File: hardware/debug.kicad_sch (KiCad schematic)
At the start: 39 parts, among them J38 Conn_01x08_Pin, J39 Conn_01x03_Pin, J40 Conn_01x08_Pin, J41 Conn_01x08_Pin, U20 74HC244, U21 74HC244, U22 74HC244

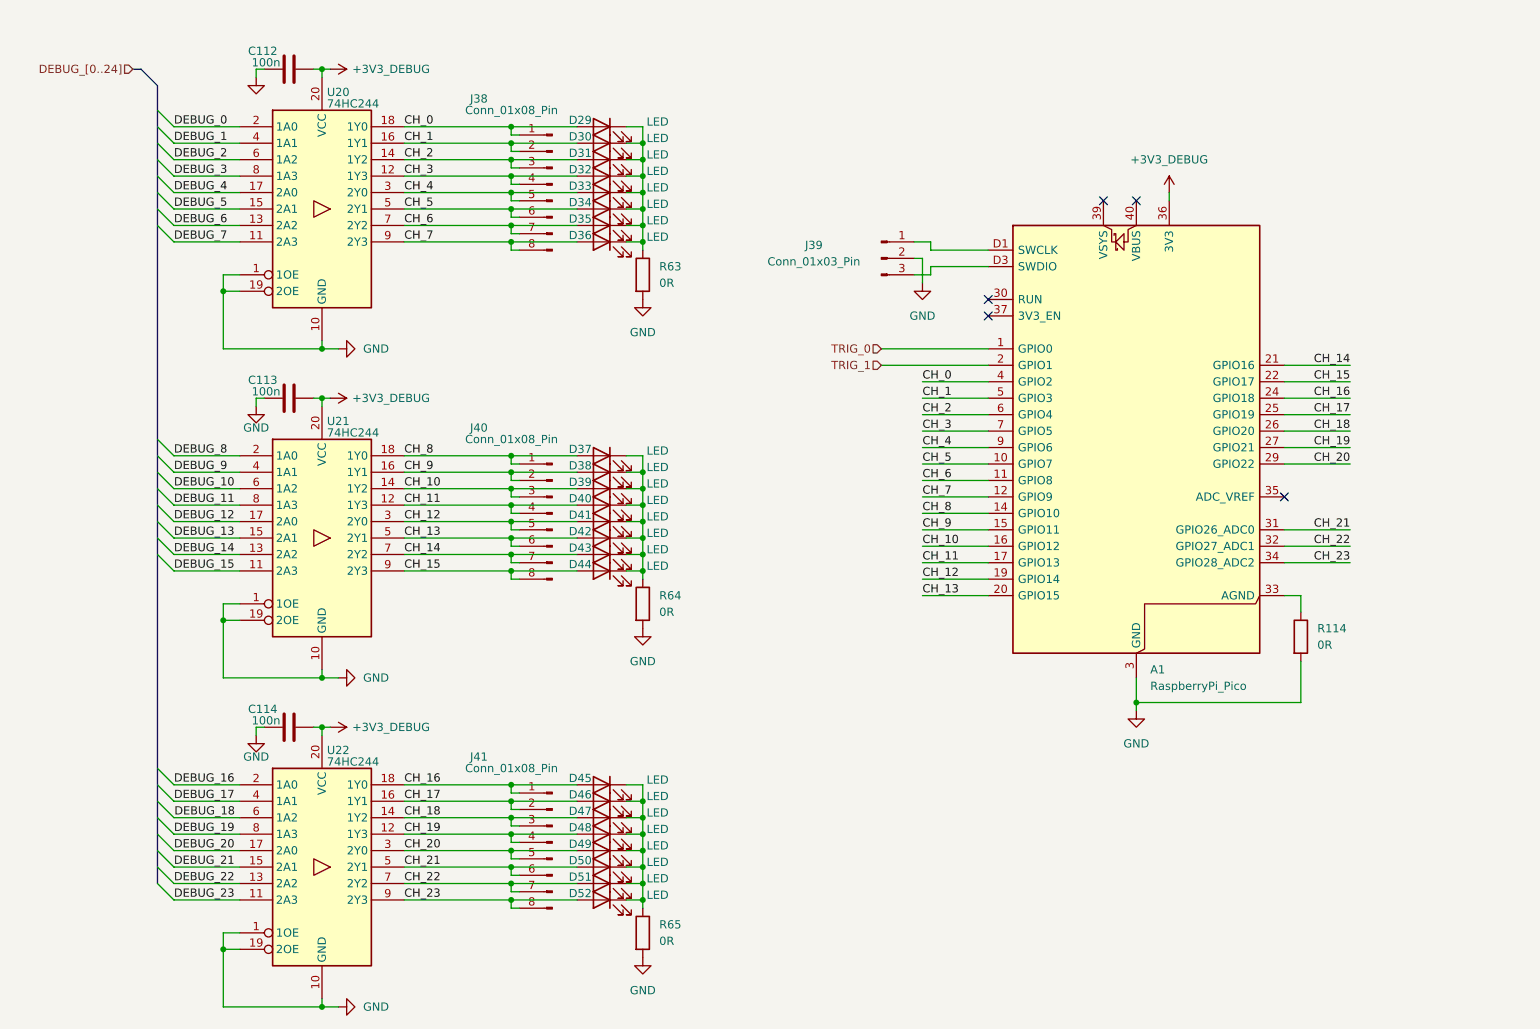
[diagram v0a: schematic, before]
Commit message: update power system + add LCSC part numbers
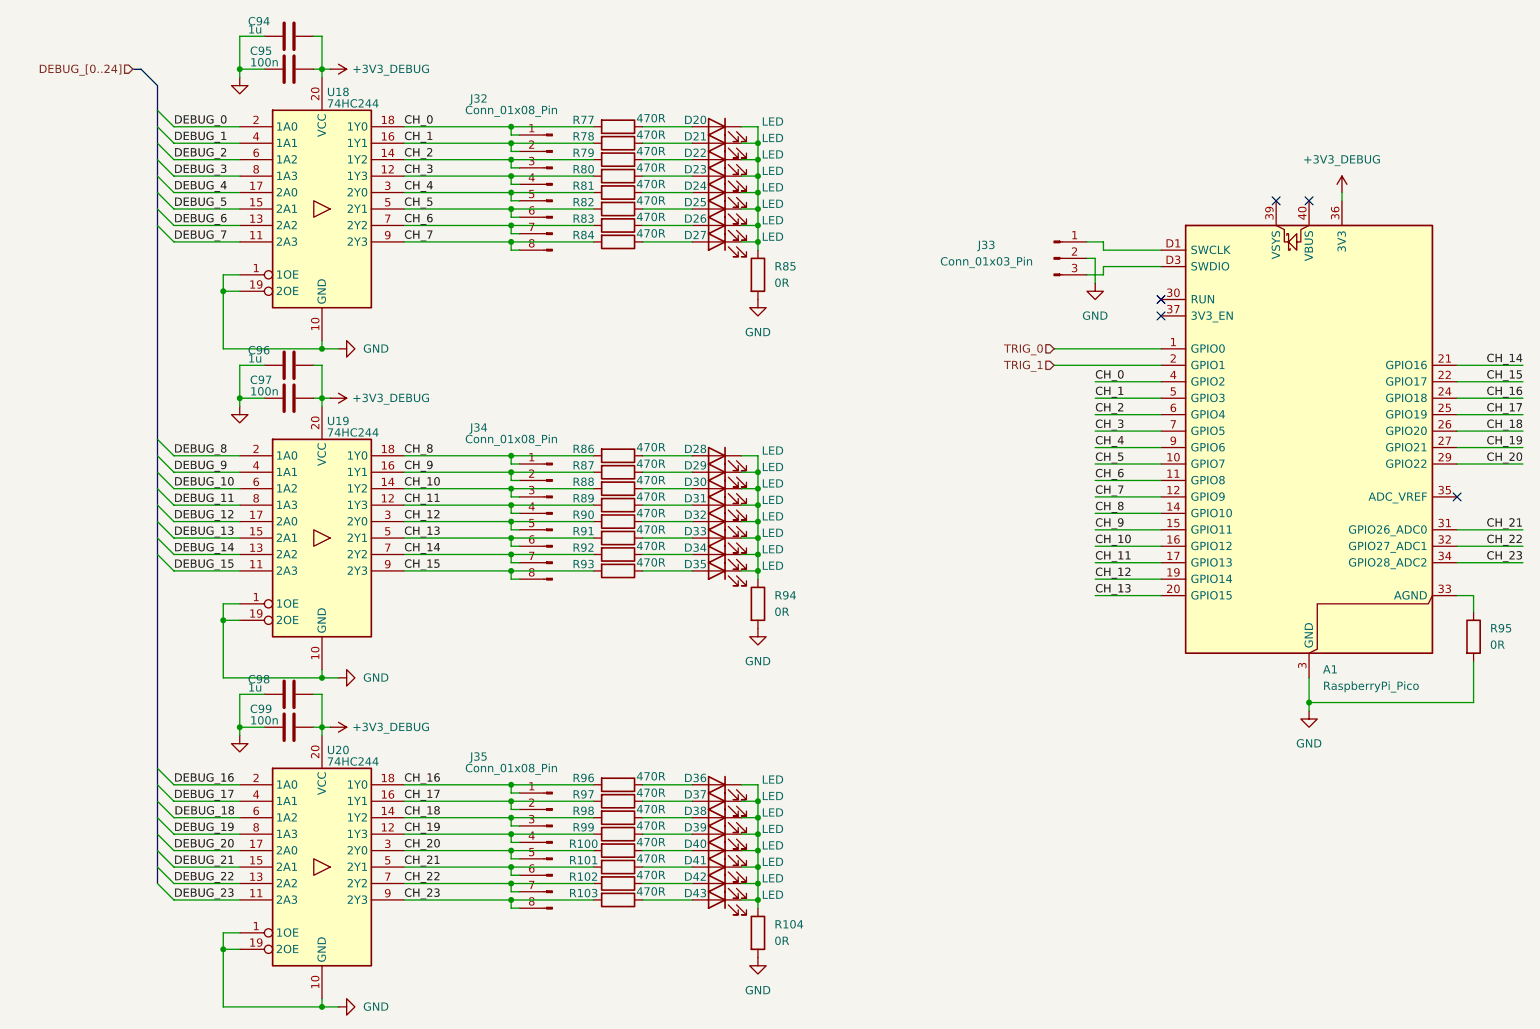
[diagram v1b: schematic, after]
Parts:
- removed C113, C114: 100n, symbol Device:C
- added C94, C96, C98: 1u, Capacitor_SMD:C_0805_2012Metric, symbol Device:C
- added C97, C99: 100n, Capacitor_SMD:C_0402_1005Metric, symbol Device:C
- added R100, R101, R102, R103, R77, R78, R79, R80, R81, R82, R83, R84, R86, R87, R88, R89, R90, R91, R92, R93, R96, R97, R98, R99: 470R, Resistor_SMD:R_0402_1005Metric, symbol Device:R
- C95: renamed from C112; footprint (none) -> Capacitor_SMD:C_0402_1005Metric; LCSC (none) -> C307331
- D20: renamed from D29; footprint (none) -> LED_SMD:LED_0805_2012Metric; LCSC (none) -> C2297
- D21: renamed from D30; footprint (none) -> LED_SMD:LED_0805_2012Metric; LCSC (none) -> C2297
- D22: renamed from D31; footprint (none) -> LED_SMD:LED_0805_2012Metric; LCSC (none) -> C2297
- D23: renamed from D32; footprint (none) -> LED_SMD:LED_0805_2012Metric; LCSC (none) -> C2297
- D24: renamed from D33; footprint (none) -> LED_SMD:LED_0805_2012Metric; LCSC (none) -> C2297
- D25: renamed from D34; footprint (none) -> LED_SMD:LED_0805_2012Metric; LCSC (none) -> C2297
- D26: renamed from D35; footprint (none) -> LED_SMD:LED_0805_2012Metric; LCSC (none) -> C2297
- D27: renamed from D36; footprint (none) -> LED_SMD:LED_0805_2012Metric; LCSC (none) -> C2297
- D28: renamed from D37; footprint (none) -> LED_SMD:LED_0805_2012Metric; LCSC (none) -> C2297
- D29: renamed from D38; footprint (none) -> LED_SMD:LED_0805_2012Metric; LCSC (none) -> C2297
- D30: renamed from D39; footprint (none) -> LED_SMD:LED_0805_2012Metric; LCSC (none) -> C2297
- D31: renamed from D40; footprint (none) -> LED_SMD:LED_0805_2012Metric; LCSC (none) -> C2297
- D32: renamed from D41; footprint (none) -> LED_SMD:LED_0805_2012Metric; LCSC (none) -> C2297
- D33: renamed from D42; footprint (none) -> LED_SMD:LED_0805_2012Metric; LCSC (none) -> C2297
- D34: renamed from D43; footprint (none) -> LED_SMD:LED_0805_2012Metric; LCSC (none) -> C2297
- D35: renamed from D44; footprint (none) -> LED_SMD:LED_0805_2012Metric; LCSC (none) -> C2297
- D36: renamed from D45; footprint (none) -> LED_SMD:LED_0805_2012Metric; LCSC (none) -> C2297
- D37: renamed from D46; footprint (none) -> LED_SMD:LED_0805_2012Metric; LCSC (none) -> C2297
- D38: renamed from D47; footprint (none) -> LED_SMD:LED_0805_2012Metric; LCSC (none) -> C2297
- D39: renamed from D48; footprint (none) -> LED_SMD:LED_0805_2012Metric; LCSC (none) -> C2297
- D40: renamed from D49; footprint (none) -> LED_SMD:LED_0805_2012Metric; LCSC (none) -> C2297
- D41: renamed from D50; footprint (none) -> LED_SMD:LED_0805_2012Metric; LCSC (none) -> C2297
- D42: renamed from D51; footprint (none) -> LED_SMD:LED_0805_2012Metric; LCSC (none) -> C2297
- D43: renamed from D52; footprint (none) -> LED_SMD:LED_0805_2012Metric; LCSC (none) -> C2297
- J32: renamed from J38; footprint (none) -> Connector_PinHeader_2.54mm:PinHeader_1x08_P2.54mm_Vertical
- J33: renamed from J39; footprint (none) -> Connector_PinHeader_2.54mm:PinHeader_1x03_P2.54mm_Vertical
- J34: renamed from J40; footprint (none) -> Connector_PinHeader_2.54mm:PinHeader_1x08_P2.54mm_Vertical
- J35: renamed from J41; footprint (none) -> Connector_PinHeader_2.54mm:PinHeader_1x08_P2.54mm_Vertical
- R104: renamed from R65; footprint (none) -> Resistor_SMD:R_0402_1005Metric; LCSC (none) -> C17168
- R85: renamed from R63; footprint (none) -> Resistor_SMD:R_0402_1005Metric; LCSC (none) -> C17168
- R94: renamed from R64; footprint (none) -> Resistor_SMD:R_0402_1005Metric; LCSC (none) -> C17168
- R95: renamed from R114; footprint (none) -> Resistor_SMD:R_0402_1005Metric; LCSC (none) -> C17168
- U18: renamed from U20; footprint (none) -> Package_SO:TSSOP-20_4.4x6.5mm_P0.65mm; LCSC (none) -> C6835
- U19: renamed from U21; footprint (none) -> Package_SO:TSSOP-20_4.4x6.5mm_P0.65mm; LCSC (none) -> C6835
- U20: renamed from U22; footprint (none) -> Package_SO:TSSOP-20_4.4x6.5mm_P0.65mm; LCSC (none) -> C6835
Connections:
- net +3V3_DEBUG: now also C94.2, C96.2, C97.2, C98.2, C99.2
- net CH_0: now also R77.2; no longer D20.2 (A)
- net CH_1: now also R78.2; no longer D21.2 (A)
- net CH_10: now also R88.2; no longer D30.2 (A)
- net CH_11: now also R89.2; no longer D31.2 (A)
- net CH_12: now also R90.2; no longer D32.2 (A)
- net CH_13: now also R91.2; no longer D33.2 (A)
- net CH_14: now also R92.2; no longer D34.2 (A)
- net CH_15: now also R93.2; no longer D35.2 (A)
- net CH_16: now also R96.2; no longer D36.2 (A)
- net CH_17: now also R97.2; no longer D37.2 (A)
- net CH_18: now also R98.2; no longer D38.2 (A)
- net CH_19: now also R99.2; no longer D39.2 (A)
- net CH_2: now also R79.2; no longer D22.2 (A)
- net CH_20: now also R100.2; no longer D40.2 (A)
- net CH_21: now also R101.2; no longer D41.2 (A)
- net CH_22: now also R102.2; no longer D42.2 (A)
- net CH_23: now also R103.2; no longer D43.2 (A)
- net CH_3: now also R80.2; no longer D23.2 (A)
- net CH_4: now also R81.2; no longer D24.2 (A)
- net CH_5: now also R82.2; no longer D25.2 (A)
- net CH_6: now also R83.2; no longer D26.2 (A)
- net CH_7: now also R84.2; no longer D27.2 (A)
- net CH_8: now also R86.2; no longer D28.2 (A)
- net CH_9: now also R87.2; no longer D29.2 (A)
- net GND: now also C94.1, C96.1, C97.1, C98.1, C99.1
- new net: D24.2 (A), R81.1
- new net: D42.2 (A), R102.1
- new net: D21.2 (A), R78.1
- new net: D39.2 (A), R99.1
- new net: D32.2 (A), R90.1
- new net: D30.2 (A), R88.1
- new net: D38.2 (A), R98.1
- new net: D34.2 (A), R92.1
- new net: D40.2 (A), R100.1
- new net: D26.2 (A), R83.1
- new net: D27.2 (A), R84.1
- new net: D41.2 (A), R101.1
- new net: D20.2 (A), R77.1
- new net: D43.2 (A), R103.1
- new net: D25.2 (A), R82.1
- new net: D36.2 (A), R96.1
- new net: D35.2 (A), R93.1
- new net: D28.2 (A), R86.1
- new net: D23.2 (A), R80.1
- new net: D31.2 (A), R89.1
- new net: D22.2 (A), R79.1
- new net: D29.2 (A), R87.1
- new net: D37.2 (A), R97.1
- new net: D33.2 (A), R91.1
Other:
- moved on the sheet: A1, D20, D21, D22, D23, D24, D25, D26, D27, D28, D29, D30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

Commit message: apply manufacturing BOM
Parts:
- renumbered C96 to C100, C97 to C101, C98 to C102, C99 to C103, C94 to C98, C95 to C99, J32 to J31, J33 to J32, J34 to J33, J35 to J34, R92 to R100, R93 to R101, R94 to R102, R95 to R103, R96 to R104, R97 to R105, R98 to R106, R99 to R107, R100 to R108, R101 to R109, R102 to R110, R103 to R111, R104 to R112, R77 to R85, R78 to R86, R79 to R87, R80 to R88, R81 to R89, R82 to R90, R83 to R91, R84 to R92, R85 to R93, R86 to R94, R87 to R95, R88 to R96, R89 to R97, R90 to R98, R91 to R99

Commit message: route more
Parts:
- J31, J33, J34: footprint Connector_PinHeader_2.54mm:PinHeader_1x08_P2.54mm_Vertical -> Connector_PinHeader_1.00mm:PinHeader_1x08_P1.00mm_Vertical_SMD_Pin1Left
- J32: footprint Connector_PinHeader_2.54mm:PinHeader_1x03_P2.54mm_Vertical -> Connector_PinHeader_1.00mm:PinHeader_1x03_P1.00mm_Vertical_SMD_Pin1Left
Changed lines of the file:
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@@
 			)
 		)
-		(property "Footprint" "Connector_PinHeader_2.54mm:PinHeader_1x03_P2.54mm_Vertical"
+		(property "Footprint" "Connector_PinHeader_1.00mm:PinHeader_1x03_P1.00mm_Vertical_SMD_Pin1Left"
 			(at 187.96 64.77 0)
 			(effects
@@
 			)
 		)
-		(property "Footprint" "Connector_PinHeader_2.54mm:PinHeader_1x08_P2.54mm_Vertical"
+		(property "Footprint" "Connector_PinHeader_1.00mm:PinHeader_1x08_P1.00mm_Vertical_SMD_Pin1Left"
 			(at 110.49 104.14 0)
 			(effects
@@
 			)
 		)
-		(property "Footprint" "Connector_PinHeader_2.54mm:PinHeader_1x08_P2.54mm_Vertical"
+		(property "Footprint" "Connector_PinHeader_1.00mm:PinHeader_1x08_P1.00mm_Vertical_SMD_Pin1Left"
 			(at 110.49 154.94 0)
 			(effects
@@
 			)
 		)
-		(property "Footprint" "Connector_PinHeader_2.54mm:PinHeader_1x08_P2.54mm_Vertical"
+		(property "Footprint" "Connector_PinHeader_1.00mm:PinHeader_1x08_P1.00mm_Vertical_SMD_Pin1Left"
 			(at 110.49 53.34 0)
 			(effects

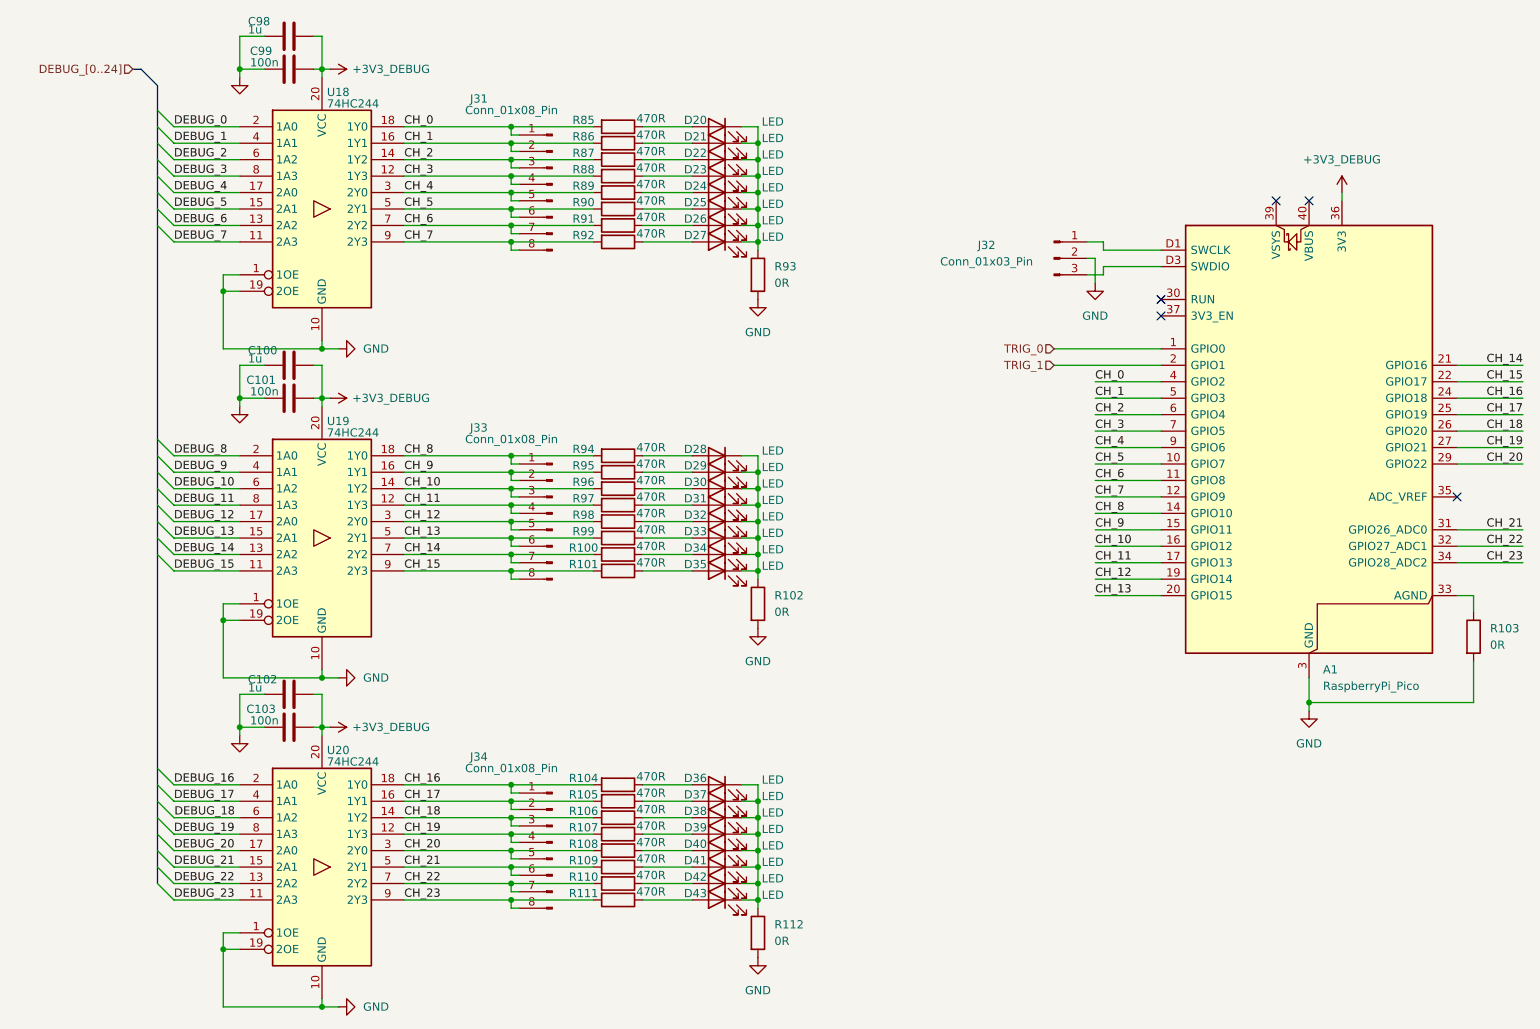
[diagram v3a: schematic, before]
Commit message: wire until sipm power
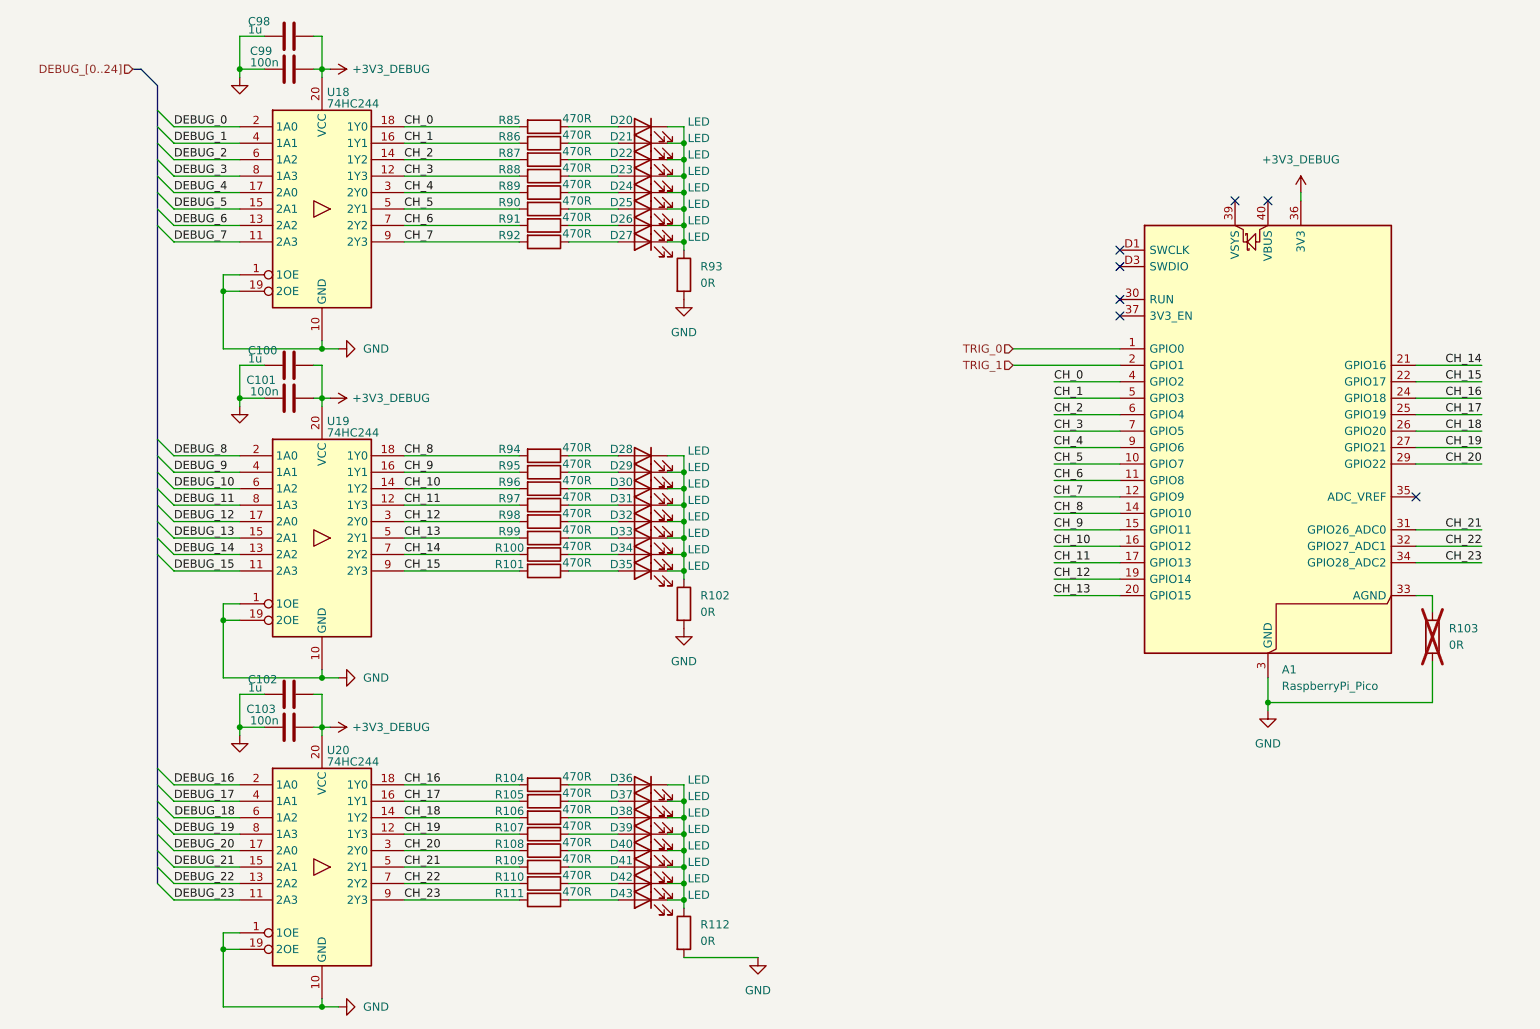
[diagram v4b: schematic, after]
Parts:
- removed J31, J33, J34: Conn_01x08_Pin, Connector_PinHeader_1.00mm:PinHeader_1x08_P1.00mm_Vertical_SMD_Pin1Left, symbol Connector:Conn_01x08_Pin
- removed J32: Conn_01x03_Pin, Connector_PinHeader_1.00mm:PinHeader_1x03_P1.00mm_Vertical_SMD_Pin1Left, symbol Connector:Conn_01x03_Pin
- R103: now not fitted
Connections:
- no-connect marks 5 -> 7
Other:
- moved on the sheet: A1, D20, D21, D22, D23, D24, D25, D26, D27, D28, D29, D30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

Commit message: route
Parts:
- renumbered C98 to C68, C99 to C69, C100 to C70, C101 to C71, C102 to C72, C103 to C73, D20 to D14, D21 to D15, D22 to D16, D23 to D17, D24 to D18, D25 to D19, D26 to D20, D27 to D21, D28 to D22, D29 to D23, D30 to D24, D31 to D25, D32 to D26, D33 to D27, D34 to D28, D35 to D29, D36 to D30, D37 to D31, D38 to D32, D39 to D33, D40 to D34, D41 to D35, D42 to D36, D43 to D37, R85 to R61, R86 to R62, R87 to R63, R88 to R64, R89 to R65, R90 to R66, R91 to R67, R92 to R68, R93 to R69, R94 to R70, R95 to R71, R96 to R72, R97 to R73, R98 to R74, R99 to R75, R100 to R76, R101 to R77, R102 to R78, R103 to R79, R104 to R80, R105 to R81, R106 to R82, R107 to R83, R108 to R84, R109 to R85, R110 to R86, R111 to R87, R112 to R88, U18 to U11, U19 to U12, U20 to U13
